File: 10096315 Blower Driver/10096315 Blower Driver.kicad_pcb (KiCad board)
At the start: 4 copper layers, 92.5 x 72 mm, 142 parts, among them IC1 MotorDriver, IC2 NE555D, IC3 HighSideDriver, IC4 HighSideDriver, IC5 HighSideDriver, IC6 LinearRegulator, J1 2pinConnector_Power, J11 2pinConnector_Unknown, J2 10pinConnector, J22 9pinConnector, J3 2pinConnector, J4 JumperBypass, J6 8pinConnector, T1 MOSFET_NMOS_30V, T10 MOSFET_NMOS_30V, T2 MOSFET_NMOS_55V, T3 MOSFET_NMOS_55V, T4 MOSFET_NMOS_55V, T5 MOSFET_NMOS_55V, T6 MOSFET_NMOS_30V, T7 MOSFET_NMOS_55V, T8 MOSFET_NMOS_55V, T9 MOSFET_PMOS_60V

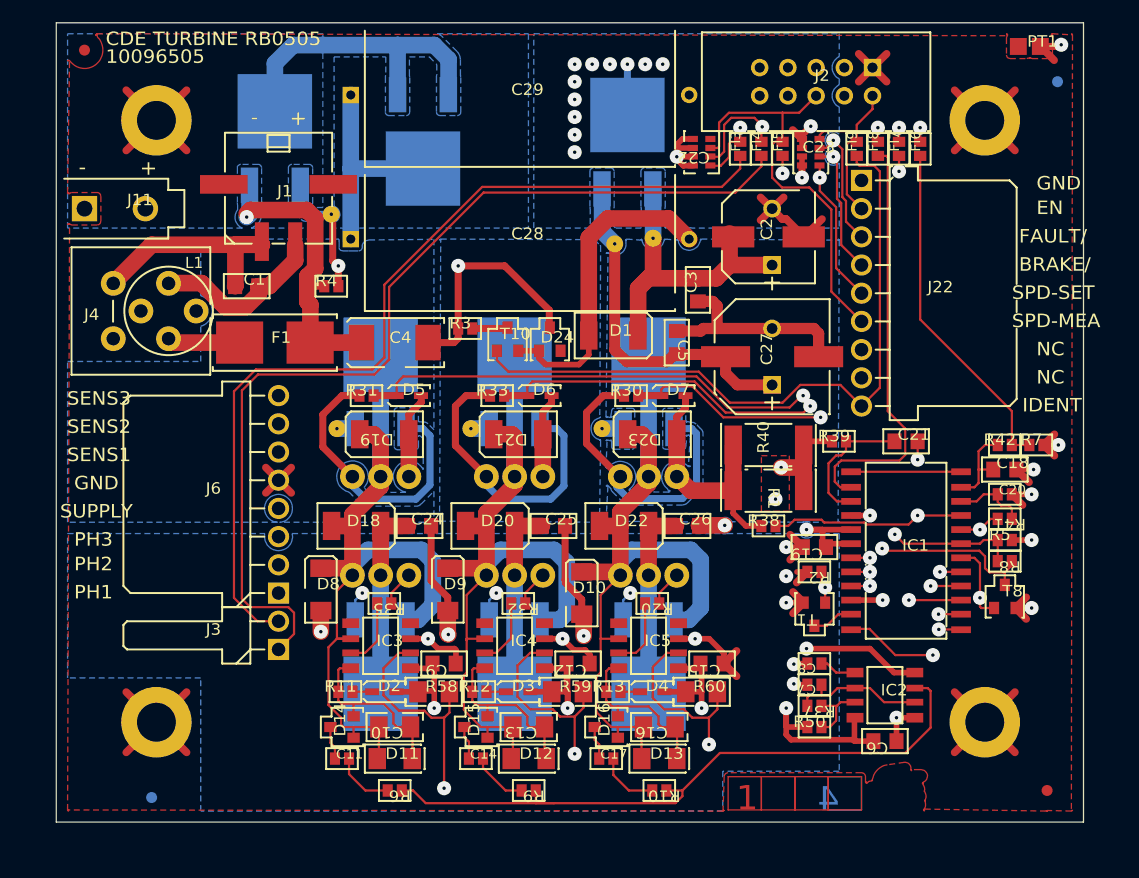
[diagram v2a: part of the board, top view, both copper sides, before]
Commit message: Fixed footprint/symbol pin orientation, assigned missing nets to all tracks and pours
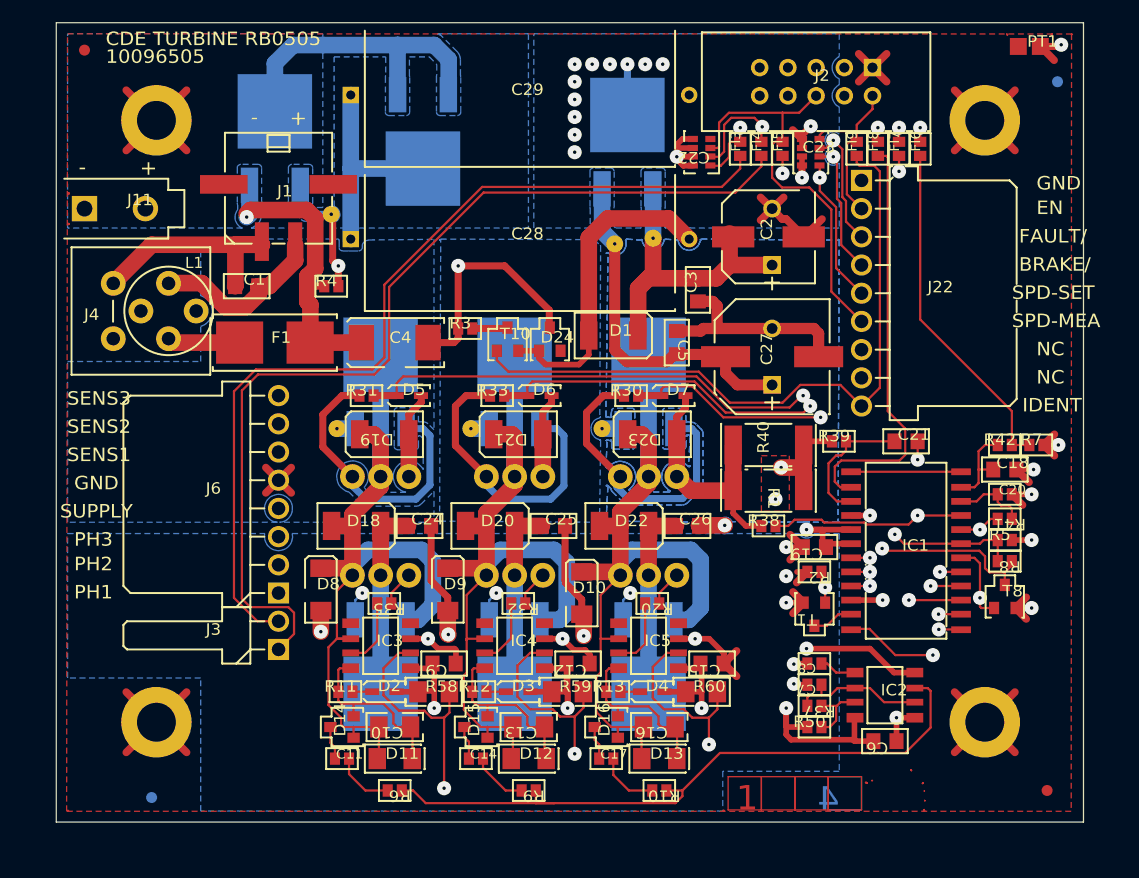
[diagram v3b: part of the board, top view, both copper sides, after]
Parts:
- T6: value MOSFET_NMOS_30V -> MOSFET_NMOS_55V
- T8: value MOSFET_NMOS_55V -> MOSFET_NMOS_30V
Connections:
- ? pad : (no net) -> Net-(C4-Pad-)
- ? pad : (no net) -> /ISENS (x3)
- ? pad : (no net) -> +15V
- ? pad : (no net) -> +24V
- C10 pad 1: Net-(C10-Pad1) -> /PHA3
- C12 pad 1: +15V -> GND
- C12 pad 2: GND -> +15V
- C13 pad 1: Net-(C13-Pad1) -> /PHA2
- C15 pad 1: +15V -> GND
- C15 pad 2: GND -> +15V
- C16 pad 1: Net-(C16-Pad1) -> /PHA1
- C19 pad 1: GND -> +15V
- C19 pad 2: +15V -> GND
- C2 pad +: GND -> +24V
- C2 pad -: +24V -> GND
- C20 pad 1: Net-(C20-Pad1) -> GND
- C20 pad 2: GND -> Net-(C20-Pad2)
- C24 pad 1: GNDPWR -> +24V
- C24 pad 2: +24V -> GNDPWR
- C25 pad 1: GNDPWR -> +24V
- C25 pad 2: +24V -> GNDPWR
- C26 pad 1: GNDPWR -> +24V
- C26 pad 2: +24V -> GNDPWR
- C3 pad 1: +24V -> GND
- C3 pad 2: GND -> +24V
- C5 pad 1: +15V -> GND
- C5 pad 2: GND -> +15V
- C6 pad 1: +15V -> GND
- C6 pad 2: GND -> +15V
- C7 pad 1: Net-(C7-Pad1) -> GND
- C7 pad 2: GND -> Net-(C7-Pad2)
- C8 pad 1: Net-(C8-Pad1) -> GND
- C8 pad 2: GND -> Net-(C8-Pad2)
- C9 pad 1: +15V -> GND
- C9 pad 2: GND -> +15V
- D14 pad 1: Net-(C10-Pad2) -> /PHA3
- D14 pad 2: Net-(C10-Pad1) -> Net-(C10-Pad2)
- D15 pad 1: Net-(C13-Pad2) -> /PHA2
- D15 pad 2: Net-(C13-Pad1) -> Net-(C13-Pad2)
- D16 pad 1: Net-(C16-Pad2) -> /PHA1
- D16 pad 2: Net-(C16-Pad1) -> Net-(C16-Pad2)
- D2 pad A: +15V -> (no net)
- D2 pad K: Net-(D2-PadK) -> (no net)
- D3 pad A: +15V -> (no net)
- D3 pad K: Net-(D3-PadK) -> (no net)
- D4 pad A: +15V -> (no net)
- D4 pad K: Net-(D4-PadK) -> (no net)
- D5 pad A: /ISENS -> (no net)
- D5 pad K: /BOT-DR-C -> (no net)
- D6 pad A: /ISENS -> (no net)
- D6 pad K: /BOT-DR-B -> (no net)
- D7 pad A: /ISENS -> (no net)
- D7 pad K: /BOT-DR-A -> (no net)
- F1 pad 1: Net-(C4-Pad+) -> Net-(F1-Pad1)
- F1 pad 2: Net-(F1-Pad2) -> Net-(C4-Pad+)
- FI1 pad B: Net-(C1-Pad1) -> Net-(C1-Pad2)
- FI1 pad CB: Net-(F1-Pad2) -> Net-(F1-Pad1)
- FI1 pad PSG: Net-(C1-Pad2) -> Net-(C1-Pad1)
- FI3 pad 1: /TEMP+ -> Net-(C22-Pad1)
- FI3 pad 2: Net-(C22-Pad1) -> /TEMP+
- FI4 pad 1: /TEMP- -> Net-(C22-Pad2)
- FI4 pad 2: Net-(C22-Pad2) -> /TEMP-
- FI5 pad 1: Net-(FI5-Pad1) -> Net-(C22-Pad3)
- FI5 pad 2: Net-(C22-Pad3) -> Net-(FI5-Pad2)
- FI6 pad 1: Net-(FI6-Pad1) -> Net-(C23-Pad5)
- FI6 pad 2: Net-(C23-Pad5) -> Net-(FI6-Pad2)
- FI7 pad 1: Net-(FI7-Pad1) -> Net-(C23-Pad6)
- FI7 pad 2: Net-(C23-Pad6) -> Net-(FI7-Pad2)
- FI8 pad 1: Net-(FI8-Pad1) -> Net-(C23-Pad7)
- FI8 pad 2: Net-(C23-Pad7) -> Net-(FI8-Pad2)
- FI9 pad 1: /OE -> Net-(C23-Pad8)
- FI9 pad 2: Net-(C23-Pad8) -> /OE
- IC1 pad 10: Net-(C20-Pad1) -> Net-(C20-Pad2)
- IC1 pad 14: Net-(FI8-Pad1) -> Net-(FI8-Pad2)
- IC1 pad 15: Net-(C21-Pad2) -> Net-(C21-Pad1)
- IC1 pad 9: Net-(C21-Pad1) -> Net-(C21-Pad2)
- IC2 pad 2: Net-(C7-Pad1) -> Net-(C7-Pad2)
- IC2 pad 5: Net-(C8-Pad1) -> Net-(C8-Pad2)
- IC2 pad 6: Net-(C7-Pad1) -> Net-(C7-Pad2)
- IC3 pad 6: Net-(C10-Pad2) -> /PHA3
- IC3 pad 8: Net-(C10-Pad1) -> Net-(C10-Pad2)
- IC4 pad 6: Net-(C13-Pad2) -> /PHA2
- IC4 pad 8: Net-(C13-Pad1) -> Net-(C13-Pad2)
- IC5 pad 6: Net-(C16-Pad2) -> /PHA1
- IC5 pad 8: Net-(C16-Pad1) -> Net-(C16-Pad2)
- J1 pad 1: Net-(C1-Pad2) -> Net-(C1-Pad1)
- J1 pad 2: Net-(C1-Pad1) -> Net-(C1-Pad2)
- J11 pad 1: Net-(C1-Pad2) -> Net-(C1-Pad1)
- J11 pad 2: Net-(C1-Pad1) -> Net-(C1-Pad2)
- J4 pad 1: Net-(C1-Pad2) -> Net-(C1-Pad1)
- J6 pad 1: Net-(D22-PadA) -> /PHA1
- J6 pad 2: Net-(D20-PadA) -> /PHA2
- J6 pad 3: Net-(D18-PadA) -> /PHA3
- L1 pad 1: Net-(C1-Pad1) -> Net-(C1-Pad2)
- L1 pad 2: Net-(F1-Pad2) -> Net-(F1-Pad1)
- R10 pad 1: /OSC -> Net-(C17-Pad1)
- R10 pad 2: Net-(C17-Pad1) -> /OSC
- R11 pad 1: Net-(C10-Pad1) -> Net-(D2-Pad2)
- R11 pad 2: Net-(D2-PadK) -> Net-(C10-Pad2)
- R12 pad 1: Net-(C13-Pad1) -> Net-(D3-Pad2)
- R12 pad 2: Net-(D3-PadK) -> Net-(C13-Pad2)
- R13 pad 1: Net-(C16-Pad1) -> Net-(D4-Pad2)
- R13 pad 2: Net-(D4-PadK) -> Net-(C16-Pad2)
- R2 pad 1: Net-(FI7-Pad1) -> GND
- R2 pad 2: GND -> Net-(FI7-Pad2)
- R20 pad 1: Net-(R20-Pad1) -> Net-(IC5-Pad7)
- R20 pad 2: Net-(IC5-Pad7) -> Net-(R20-Pad2)
- R3 pad 1: Net-(C4-Pad-) -> Net-(R3-Pad1)
- R3 pad 2: Net-(R3-Pad2) -> Net-(C4-Pad-)
- R30 pad 1: Net-(R30-Pad1) -> /BOT-DR-A
- R30 pad 2: /BOT-DR-A -> Net-(R30-Pad2)
- R31 pad 1: Net-(R31-Pad1) -> /BOT-DR-C
- R31 pad 2: /BOT-DR-C -> Net-(R31-Pad2)
- R32 pad 1: Net-(R32-Pad1) -> Net-(IC4-Pad7)
- R32 pad 2: Net-(IC4-Pad7) -> Net-(R32-Pad2)
- R33 pad 1: Net-(R33-Pad1) -> /BOT-DR-B
- R33 pad 2: /BOT-DR-B -> Net-(R33-Pad2)
- R35 pad 1: Net-(R35-Pad1) -> Net-(IC3-Pad7)
- R35 pad 2: Net-(IC3-Pad7) -> Net-(R35-Pad2)
- R37 pad 1: Net-(IC2-Pad7) -> Net-(C7-Pad2)
- R37 pad 2: Net-(C7-Pad1) -> Net-(IC2-Pad7)
- R38 pad 1: /ISENS -> Net-(C21-Pad2)
- R38 pad 2: Net-(C21-Pad1) -> /ISENS
- R39 pad 1: GNDPWR -> Net-(C21-Pad1)
- R39 pad 2: Net-(C21-Pad2) -> GNDPWR
- R4 pad 1: Net-(C4-Pad+) -> Net-(C4-Pad-)
- R4 pad 2: Net-(C4-Pad-) -> Net-(C4-Pad+)
- R40 pad 1: /ISENS -> GNDPWR
- R40 pad 2: GNDPWR -> /ISENS
- R41 pad 2: Net-(C20-Pad1) -> Net-(C20-Pad2)
- R42 pad 1: Net-(C18-Pad1) -> Net-(FI6-Pad2)
- R42 pad 2: Net-(FI6-Pad1) -> Net-(C18-Pad1)
- R5 pad 1: /OE -> GND
- R5 pad 2: GND -> /OE
- R50 pad 1: +15V -> Net-(IC2-Pad7)
- R50 pad 2: Net-(IC2-Pad7) -> +15V
- R58 pad 1: +15V -> /TOP-DR-C
- R58 pad 2: /TOP-DR-C -> +15V
- R59 pad 1: +15V -> /TOP-DR-B
- R59 pad 2: /TOP-DR-B -> +15V
- R6 pad 1: /OSC -> Net-(C11-Pad1)
- R6 pad 2: Net-(C11-Pad1) -> /OSC
- R60 pad 1: +15V -> /TOP-DR-A
- R60 pad 2: /TOP-DR-A -> +15V
- R7 pad 1: Net-(FI6-Pad1) -> GND
- R7 pad 2: GND -> Net-(FI6-Pad2)
- R8 pad 2: Net-(FI5-Pad1) -> Net-(FI5-Pad2)
- R9 pad 1: /OSC -> Net-(C14-Pad1)
- R9 pad 2: Net-(C14-Pad1) -> /OSC
- T1 pad G: Net-(FI7-Pad1) -> Net-(FI7-Pad2)
- T10 pad D: Net-(R3-Pad2) -> Net-(R3-Pad1)
- T2 pad G: Net-(R35-Pad1) -> Net-(R35-Pad2)
- T2 pad S: Net-(D18-PadA) -> /PHA3
- T3 pad D: Net-(D18-PadA) -> /PHA3
- T3 pad G: Net-(R31-Pad1) -> Net-(R31-Pad2)
- T4 pad G: Net-(R32-Pad1) -> Net-(R32-Pad2)
- T4 pad S: Net-(D20-PadA) -> /PHA2
- T5 pad D: Net-(D20-PadA) -> /PHA2
- T5 pad G: Net-(R33-Pad1) -> Net-(R33-Pad2)
- T6 pad D: Net-(FI5-Pad1) -> +24V
- T6 pad G: /SENSOR3 -> Net-(R20-Pad2)
- T6 pad S: GND -> /PHA1
- T7 pad D: Net-(D22-PadA) -> /PHA1
- T7 pad G: Net-(R30-Pad1) -> Net-(R30-Pad2)
- T8 pad D: +24V -> Net-(FI5-Pad2)
- T8 pad G: Net-(R20-Pad1) -> /SENSOR3
- T8 pad S: Net-(D22-PadA) -> GND
- ZC2 pad +: (no net) -> +24V
- ZC2 pad -: (no net) -> GND
- ZC27 pad +: (no net) -> +15V
- ZC27 pad -: (no net) -> GND
- ZT2 pad D: (no net) -> +24V
- ZT2 pad G: (no net) -> Net-(R35-Pad2)
- ZT2 pad S: (no net) -> /PHA3
- ZT3 pad D: (no net) -> /PHA3
- ZT3 pad G: (no net) -> Net-(R31-Pad2)
- ZT3 pad S: (no net) -> /ISENS
- ZT4 pad D: (no net) -> +24V
- ZT4 pad G: (no net) -> Net-(R32-Pad2)
- ZT4 pad S: (no net) -> /PHA2
- ZT5 pad D: (no net) -> /PHA2
- ZT5 pad G: (no net) -> Net-(R33-Pad2)
- ZT5 pad S: (no net) -> /ISENS
- ZT6 pad D: (no net) -> +24V
- ZT6 pad G: (no net) -> Net-(R20-Pad2)
- ZT6 pad S: (no net) -> /PHA1
- ZT7 pad D: (no net) -> /PHA1
- ZT7 pad G: (no net) -> Net-(R30-Pad2)
- ZT7 pad S: (no net) -> /ISENS
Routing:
- net (no net): track 2389.6 -> 84.0 mm, vias 59 -> 12
- net +24V: track 2.36 -> 201.7 mm, vias 1 -> 0
- net +15V: track 4.71 -> 166.5 mm, vias 1 -> 6
- net /PHA1: track 0.00 -> 110.8 mm
- net /SENSOR3: track 0.00 -> 109.7 mm, vias 0 -> 1
- net /PHA2: track 0.00 -> 98.0 mm
- net GND: track 188.6 -> 276.7 mm, vias 9 -> 20
- net /TEMP-: track 0.00 -> 87.8 mm
- net /ISENS: track 0.00 -> 85.3 mm
- net /OE: track 1.78 -> 85.7 mm
- net /PHA3: track 0.00 -> 83.4 mm
- net /TEMP+: track 0.00 -> 82.4 mm
- net /TOP-DR-C: track 0.00 -> 80.7 mm, vias 0 -> 2
- net /BOT-DR-C: track 0.00 -> 61.4 mm, vias 0 -> 2
- net /OSC: track 0.00 -> 60.3 mm
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- added copper zone on B.Cu, net +24V
- added copper zone on B.Cu, net GND
- added copper zone on F.Cu, net GND
- added copper zone on In1.Cu, net GND
- added copper zone on In2.Cu, net GNDPWR
- added copper zone on B.Cu, net Net-(D17-PadA1)
- added copper zone on B.Cu, net Net-(D18-Pad1)
- added copper zone on B.Cu, net Net-(D20-Pad1)
- added copper zone on B.Cu, net Net-(D22-Pad1)
- removed copper zone on B.Cu, net (none)
- removed copper zone on In1.Cu, net (none)
- removed copper zone on In2.Cu, net (none)

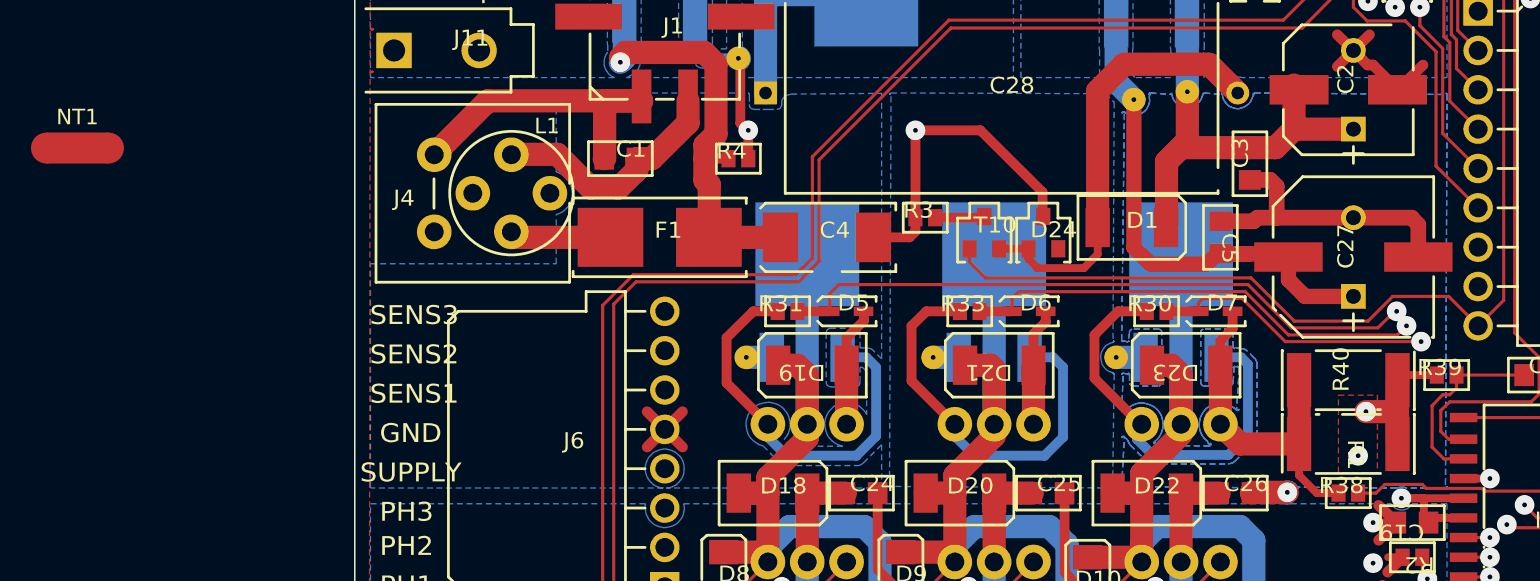
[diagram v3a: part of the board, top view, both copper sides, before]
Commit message: Added net-tie, fixed pin assignment for SOD323
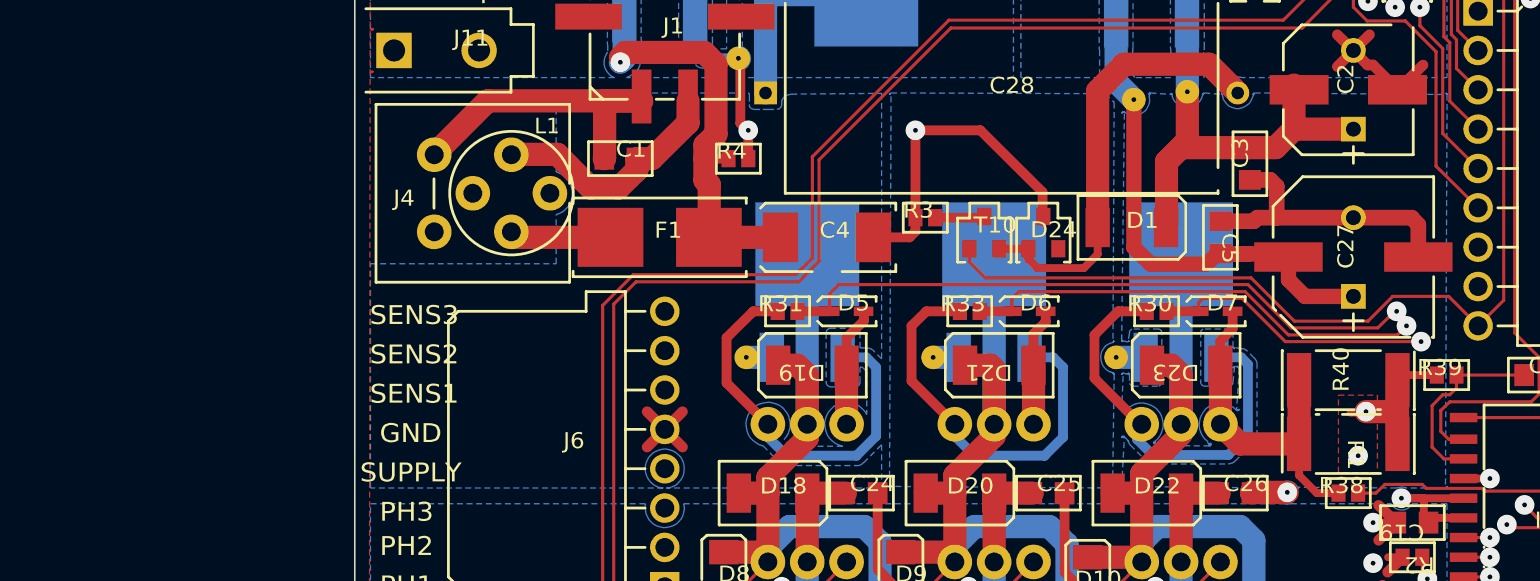
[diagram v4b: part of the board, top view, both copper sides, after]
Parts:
- NT1: footprint NetTie:NetTie-2_SMD_Pad2.0mm -> NetTie:NetTie-2_SMD_Pad0.5mm
- ZT2, ZT3, ZT4, ZT5, ZT6, ZT7: footprint TO220ABGDS-INV_COUCHE_1 -> 10096315 Blower Driver:TO220ABGDS-INV_COUCHE
- moved NT1 84.4 mm to (306.1, 40.1)
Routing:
- added copper zone on B.Cu, net /PHA1
- added copper zone on B.Cu, net /PHA2
- added copper zone on B.Cu, net /PHA3
- removed copper zone on B.Cu, net Net-(D18-Pad1)
- removed copper zone on B.Cu, net Net-(D20-Pad1)

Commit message: Fixing zones, adding first steps toward design rules
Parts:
- removed the ? at (266.1, 17.3)
- removed the ? at (266.6, 36.6)
- removed the ? at (278.6, 36.6)
- removed the ? at (290.4, 36.6)
- removed the ? at (291.6, 19.9)
- removed the ? at (295.0, 19.4)
- removed CAM5: FILM18_HORIZONTAL, FILM18_HORIZONTAL_1
- added ?: , , F.Cu at (123.3, 79.9)
- added ?: , , F.Cu at (123.8, 99.2)
- added ?: , , F.Cu at (135.9, 99.2)
- added ?: , , F.Cu at (147.7, 99.2)
- added ?: , , F.Cu at (148.9, 82.5)
- added ?: , , F.Cu at (152.3, 82.0)
- moved C19 155.9 mm to (166.8, 109.8)
- moved C2 155.9 mm to (163.0, 81.9)
- moved C21 155.9 mm to (175.1, 100.3)
- moved C24 155.9 mm to (131.3, 107.9)
- moved C25 155.9 mm to (143.3, 107.9)
- moved C27 155.9 mm to (163.0, 92.7)
- moved C7 155.9 mm to (166.8, 122.2)
- moved C8 155.9 mm to (166.8, 120.3)
- moved D17 155.9 mm to (131.6, 74.0)
- moved D24 155.9 mm to (143.0, 91.1)
- moved FI7 155.9 mm to (174.5, 74.0)
- moved FI9 155.9 mm to (170.7, 74.0)
- moved IC1 155.9 mm to (175.1, 110.2)
- moved R1 155.9 mm to (162.7, 104.8)
- moved R2 155.9 mm to (166.8, 112.1)
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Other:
- net class Covidien_1 added: clearance 0.254, trace_width 0.25, via_dia 0.8, via_drill 0.4
- board text removed: "21"

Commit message: Additional design rules added
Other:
- net class Covidien_1: trace_width 0.25 -> 0.254; via_dia 0.8 -> 1.118; via_drill 0.4 -> 0.305
- net class Default: trace_width 0.25 -> 0.254
- rule trace_min: 0.2 -> 0.254
- rule via_min_drill: 0.3 -> 0.025
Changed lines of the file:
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@@
   (page A4)
   (layers
-    (0 F.Cu signal hide)
-    (1 In1.Cu signal hide)
-    (2 In2.Cu signal hide)
+    (0 F.Cu signal)
+    (1 In1.Cu signal)
+    (2 In2.Cu signal)
     (31 B.Cu signal)
     (32 B.Adhes user)
@@
   )
   (setup
-    (last_trace_width 0.25)
+    (last_trace_width 0.254)
     (trace_clearance 0.2)
     (zone_clearance 0.2032)
     (zone_45_only no)
-    (trace_min 0.2)
+    (trace_min 0.254)
     (via_size 0.8)
     (via_drill 0.4)
     (via_min_size 0.4)
-    (via_min_drill 0.3)
+    (via_min_drill 0.025)
     (uvia_size 0.3)
     (uvia_drill 0.1)
@@
   (net_class Default "This is the default net class."
     (clearance 0.2)
-    (trace_width 0.25)
+    (trace_width 0.254)
     (via_dia 0.8)
     (via_drill 0.4)
     (uvia_dia 0.3)
     (uvia_drill 0.1)
+    (diff_pair_width 0.254)
+    (diff_pair_gap 0.25)
   )
   (net_class Covidien_1 ""
     (clearance 0.254)
-    (trace_width 0.25)
-    (via_dia 0.8)
-    (via_drill 0.4)
+    (trace_width 0.254)
+    (via_dia 1.118)
+    (via_drill 0.305)
     (uvia_dia 0.3)
     (uvia_drill 0.1)

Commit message: fix association of ZC fprints
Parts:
- ZC2: footprint C-SC8_1 -> 10096315 Blower Driver:C-SC8
- ZC27: footprint C-SC10_1 -> 10096315 Blower Driver:C-SC10
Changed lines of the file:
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@@
       (net 4 +24V))
   )
-  (module C-SC8_1 (layer F.Cu)
+  (module "10096315 Blower Driver:C-SC8" (layer F.Cu)
     (at 162.7046 81.8996 90)
     (attr smd)
@@
       (net 3 GND))
   )
-  (module C-SC10_1 (layer F.Cu)
+  (module "10096315 Blower Driver:C-SC10" (layer F.Cu)
     (at 163.0348 92.6946 90)
     (attr smd)
